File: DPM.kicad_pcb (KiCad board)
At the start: 2 copper layers, 95.9 x 90.2 mm, 19 parts, among them J1 Conn_01x08, U1 74HC590, U2 74HC682, U3 ADG333A, U4 MCP23017_SP, U5 ADG333A

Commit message: + 3 fonctionnalités : PWM, DPM & DDPM + début du routage de la carte
git-svn-id: file:///D%5C00%20-%20Dev%20&%20Calculs%5CRepoTortoiseSVN_PCB%5CD-DPM/trunk@16 f29d8339-a183-0348-962e-9e4594cf8312
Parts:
- removed U1: 74HC590, Package_DIP:DIP-16_W7.62mm_Socket_LongPads
- removed U2: 74HC682, Package_DIP:DIP-20_W7.62mm_Socket_LongPads
- added JP1: Jumper_3_Open, Connector_PinHeader_2.54mm:PinHeader_1x03_P2.54mm_Vertical, F.Cu at (54.6, 85.4)
- added JP2: Jumper_3_Open, Connector_PinHeader_2.54mm:PinHeader_1x03_P2.54mm_Vertical, F.Cu at (54.6, 80.8)
- added JP3: Jumper_3_Open, Connector_PinHeader_2.54mm:PinHeader_1x03_P2.54mm_Vertical, F.Cu at (54.6, 76.2)
- added U25: 74LS85, Package_DIP:DIP-16_W7.62mm_Socket, F.Cu at (121.9, 66.0)
- added U28: 74LS85, Package_DIP:DIP-16_W7.62mm_Socket, F.Cu at (121.9, 88.9)
- added U31: 74LS85, Package_DIP:DIP-16_W7.62mm_Socket, F.Cu at (121.9, 111.8)
- added U6: ADG333A, Package_DIP:DIP-20_W7.62mm_Socket_LongPads, F.Cu at (229.2, 95.9)
- added U8: 4040, Package_DIP:DIP-16_W7.62mm_Socket, F.Cu at (73.7, 71.1)
- J1: value Conn_01x08 -> Conn_02x12_Odd_Even; footprint Connector_PinHeader_2.54mm:PinHeader_1x08_P2.54mm_Vertical -> Connector_PinHeader_2.54mm:PinHeader_2x12_P2.54mm_Vertical
- moved U3 127.8 mm to (229.2, 65.4)
- moved U5 120.8 mm to (229.2, 80.6)
- moved U4 62.7 mm to (73.7, 111.8), turned to 180 degrees
- moved J1 12.7 mm to (86.4, 50.8), turned to 0 degrees
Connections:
- J1 pad 1: DPM -> /Q0
- J1 pad 2: Dyadic DPM -> /CNT_A0
- J1 pad 3: Gray DPM -> /CNT_A11
- J1 pad 4: unconnected-(J1-Pin_4-Pad4) -> /Q11
- J1 pad 5: unconnected-(J1-Pin_5-Pad5) -> /Q1
- J1 pad 6: I2C_A2 -> /CNT_A1
- J1 pad 7: I2C_A1 -> /CNT_A10
- J1 pad 8: I2C_A0 -> /Q10
- PCIe_SPI_1 pad 22: /Connection PCI CAN Express/~{RESET} -> ~{Reset}
- U3 pad 1: /Q6 -> unconnected-(U3-IN1-Pad1)
- U3 pad 10: /Q5 -> unconnected-(U3-IN2-Pad10)
- U3 pad 11: /Q4 -> unconnected-(U3-IN3-Pad11)
- U3 pad 12: /B3 -> /A3
- U3 pad 19: /B0 -> /A0
- U3 pad 2: /B1 -> /A1
- U3 pad 20: /Q7 -> unconnected-(U3-IN4-Pad20)
- U3 pad 9: /B2 -> /A2
- U4 pad 1: /B0 -> /A8
- U4 pad 15: I2C_A0 -> Net-(JP3-C)
- U4 pad 16: I2C_A1 -> Net-(JP2-C)
- U4 pad 17: I2C_A2 -> Net-(JP1-C)
- U4 pad 18: VCC -> ~{Reset}
- U4 pad 2: /B1 -> /A9
- U4 pad 21: Net-(U2-Q0) -> /A0
- U4 pad 22: Net-(U2-Q1) -> /A1
- U4 pad 23: Net-(U2-Q2) -> /A2
- U4 pad 24: Net-(U2-Q3) -> /A3
- U4 pad 25: Net-(U2-Q4) -> /A4
- U4 pad 26: Net-(U2-Q5) -> /A5
- U4 pad 27: Net-(U2-Q6) -> /A6
- U4 pad 28: Net-(U2-Q7) -> /A7
- U4 pad 3: /B2 -> /A10
- U4 pad 4: /B3 -> /A11
- U4 pad 5: /B4 -> PreScaler0
- U4 pad 6: /B5 -> PreScaler1
- U4 pad 7: /B6 -> PreScaler2
- U4 pad 8: /B7 -> ~{CntEN}
- U5 pad 1: /Q0 -> unconnected-(U5-IN1-Pad1)
- U5 pad 10: /Q3 -> unconnected-(U5-IN2-Pad10)
- U5 pad 11: /Q2 -> unconnected-(U5-IN3-Pad11)
- U5 pad 12: /B5 -> /A7
- U5 pad 17: Net-(U5-D3) -> Net-(U3-D3)
- U5 pad 19: /B6 -> /A4
- U5 pad 2: /B7 -> /A5
- U5 pad 20: /Q1 -> unconnected-(U5-IN4-Pad20)
- U5 pad 3: Dyadic DPM -> Net-(U5-D1)
- U5 pad 7: Net-(U3-D3) -> Net-(U5-D1)
- U5 pad 9: /B4 -> /A6
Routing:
- net Ground: track 421.7 -> 211.3 mm
- net VCC: track 326.1 -> 161.0 mm
- net /A11: track 0.00 -> 110.9 mm
- net /A0: track 0.00 -> 92.1 mm
- net /CNT_A11: track 0.00 -> 91.2 mm
- net /B5: track 90.9 -> 0.00 mm
- net /A1: track 0.00 -> 89.2 mm
- net /A3: track 0.00 -> 87.3 mm
- net /B3: track 85.5 -> 0.00 mm
- net /A2: track 0.00 -> 84.1 mm
- net /A9: track 0.00 -> 82.9 mm
- net /B1: track 82.1 -> 0.00 mm
- net /B0: track 80.8 -> 0.00 mm
- net /CNT_A10: track 0.00 -> 79.4 mm
- net Dyadic DPM: track 79.4 -> 0.00 mm
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- added copper zone on F.Cu, net Ground
- removed copper zone on F.Cu, net VCC
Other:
- board text removed: "COPI"

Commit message: POPOPO !!!!! 1ere version du routage de la carte
git-svn-id: file:///D%5C00%20-%20Dev%20&%20Calculs%5CRepoTortoiseSVN_PCB%5CD-DPM/trunk@17 f29d8339-a183-0348-962e-9e4594cf8312
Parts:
- removed PCIe_CAN_1: Conn_02x07_Odd_Even, Connector_PinHeader_2.54mm:PinHeader_2x07_P2.54mm_Vertical
- removed PCIe_SPI_1: Conn_02x11_Odd_Even, Connector_PinHeader_2.54mm:PinHeader_2x11_P2.54mm_Vertical
- added JP4: IDC-14, Connector_IDC:IDC-Header_2x07_P2.54mm_Horizontal, F.Cu at (58.4, 114.3)
- moved U3 113.7 mm to (116.8, 48.3), turned to 0 degrees
- moved U6 112.7 mm to (116.8, 104.1), turned to 0 degrees
- moved U5 112.5 mm to (116.8, 76.2), turned to 0 degrees
- moved U25 13.0 mm to (109.2, 68.6)
- moved U28 13.0 mm to (109.2, 91.4)
- moved U31 13.0 mm to (109.2, 114.3)
- moved R5 7.57 mm to (72.7, 118.1)
- moved LED1 6.67 mm to (66.0, 118.1)
- moved JP1 6.43 mm to (48.3, 86.4)
- moved JP2 6.37 mm to (48.3, 81.3)
- moved JP3 6.35 mm to (48.3, 76.2)
- moved U4 5.08 mm to (78.7, 111.8)
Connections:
- net VCC renamed +5V
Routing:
- net Ground: track 211.3 -> 541.8 mm
- net +5V: track 161.0 -> 399.4 mm
- net DPM: track 0.00 -> 51.0 mm
- net /A9: track 82.9 -> 43.7 mm
- net /A11: track 110.9 -> 75.0 mm
- net Clock: track 37.9 -> 65.1 mm
- net /A8: track 57.7 -> 80.8 mm
- net ~{Reset}: track 20.7 -> 40.7 mm
- net /A5: track 77.3 -> 60.9 mm
- net unconnected-(U3-IN4-Pad20): track 16.3 -> 0.00 mm
- net unconnected-(U6-IN3-Pad11): track 16.3 -> 0.00 mm
- net /CNT_A3: track 26.5 -> 12.7 mm
- net /CNT_A2: track 26.5 -> 12.7 mm
- net Net-(JP2-C): track 10.1 -> 23.5 mm
- net /CNT_A11: track 91.2 -> 78.1 mm
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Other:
- board text removed: "+3.3V"
- board text removed: "CAN0 H"
- board text removed: "CAN0 L"
- board text removed: "CAN1 H"
- board text removed: "CAN1 L"
- board text removed: "CIPO"
- board text removed: "OSC1"
- board text removed: "OSC2"
- board text removed: "SCLK"
- board text removed: "~{CS1}"
- board text removed: "~{CS2}"
- board text removed: "~{CS3}"

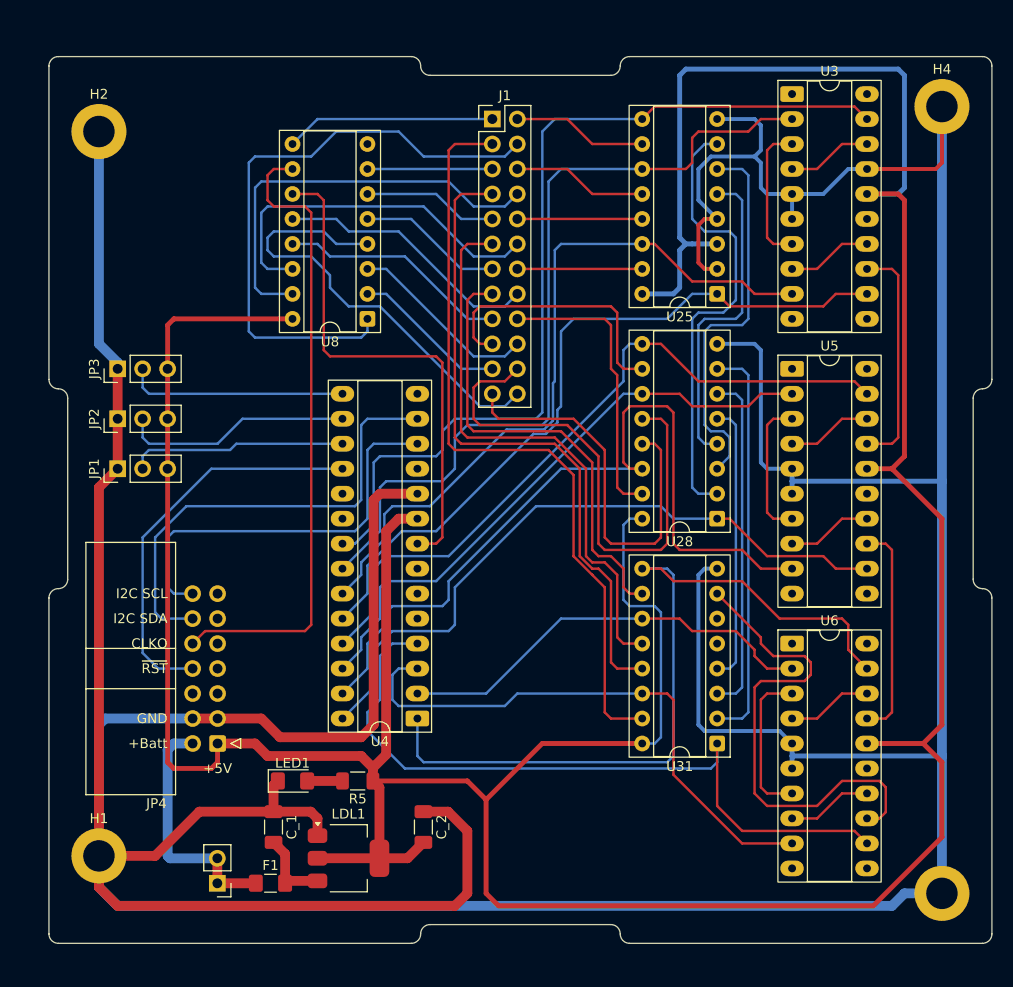
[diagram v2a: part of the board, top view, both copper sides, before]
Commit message: Ajout du prescaler TODO : - condensateurs de découplage - bouchon I2C
git-svn-id: file:///D%5C00%20-%20Dev%20&%20Calculs%5CRepoTortoiseSVN_PCB%5CD-DPM/trunk@18 f29d8339-a183-0348-962e-9e4594cf8312
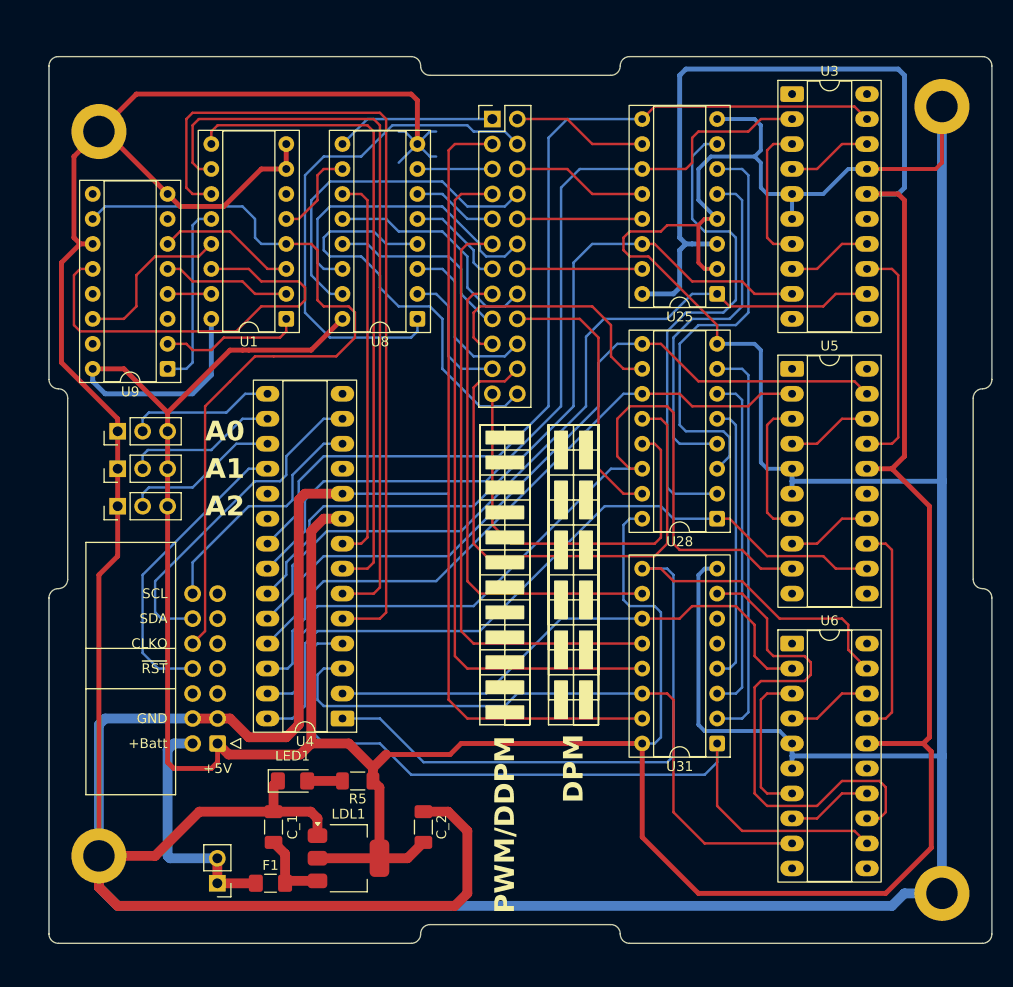
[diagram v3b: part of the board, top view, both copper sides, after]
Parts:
- added U1: 74LS251, Package_DIP:DIP-16_W7.62mm_Socket, F.Cu at (65.4, 71.1)
- added U9: 4040, Package_DIP:DIP-16_W7.62mm_Socket, F.Cu at (53.3, 76.2)
- moved U4 7.62 mm to (71.1, 111.8)
- moved JP3 6.35 mm to (48.3, 82.5)
- moved JP2 5.08 mm to (48.3, 86.4)
- moved U8 5.08 mm to (78.7, 71.1)
- moved JP1 3.81 mm to (48.3, 90.2)
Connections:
- U8 pad 10: Clock -> Net-(U1-Y)
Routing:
- net Ground: track 541.8 -> 650.9 mm
- net PreScaler0: track 0.00 -> 85.5 mm
- net PreScaler1: track 0.00 -> 76.6 mm
- net PreScaler2: track 0.00 -> 65.6 mm
- net /Div_512: track 0.00 -> 43.9 mm
- net /Div_4096: track 0.00 -> 18.9 mm
- net /Div_1024: track 0.00 -> 17.1 mm
- net SCL: track 41.3 -> 24.9 mm
- net Clock: track 65.1 -> 81.1 mm
- net /Div_64: track 0.00 -> 14.4 mm
- net /Div_8: track 0.00 -> 14.2 mm
- net SDA: track 47.8 -> 34.3 mm
- net /Div_16: track 0.00 -> 13.1 mm
- net ~{CntEN}: track 51.9 -> 39.9 mm
- net /A9: track 43.7 -> 53.9 mm
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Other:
- board text added: "A0"
- board text added: "A1"
- board text added: "A2"
- board text added: "DPM"
- board text added: "PWM/DDPM"
- board text added: "SCL"
- board text added: "SDA"
- board text removed: "I2C SCL"
- board text removed: "I2C SDA"

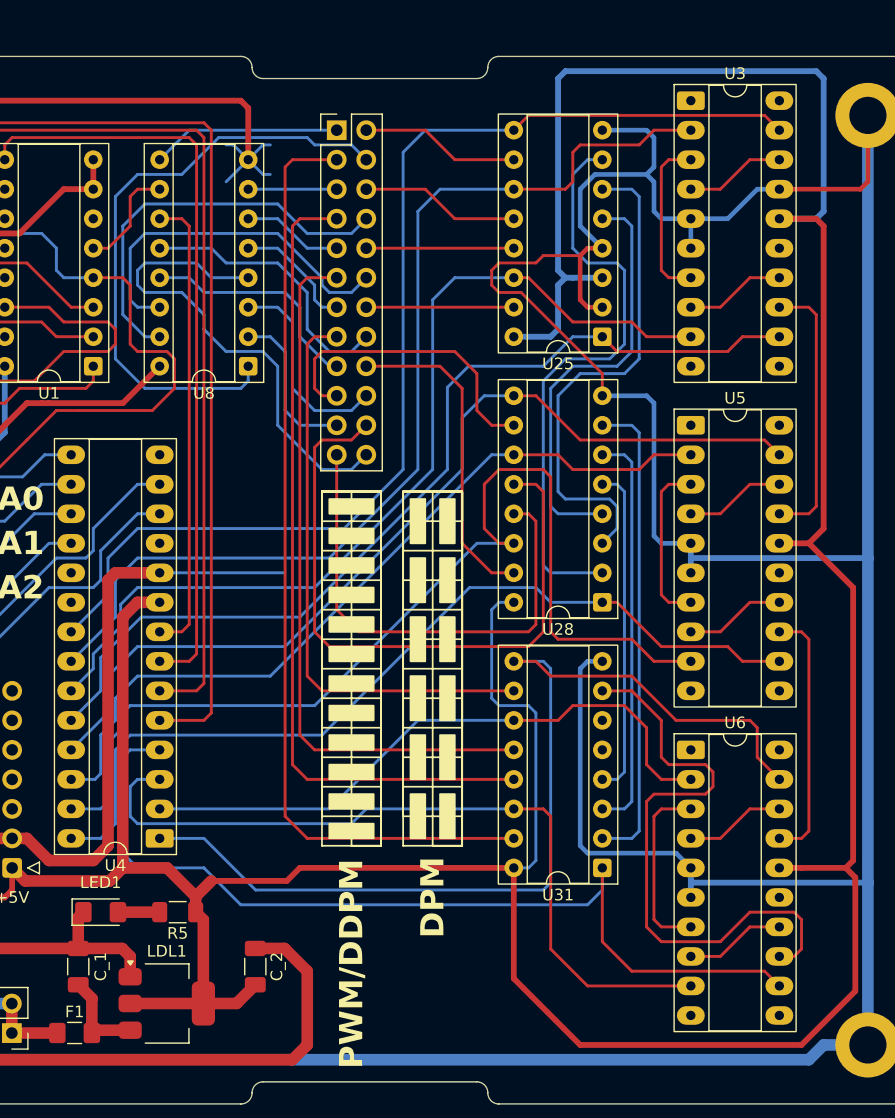
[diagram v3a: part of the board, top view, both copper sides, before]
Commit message: Début de ré&vision pour ajouter des câblages
git-svn-id: file:///D%5C00%20-%20Dev%20&%20Calculs%5CRepoTortoiseSVN_PCB%5CD-DPM/trunk@19 f29d8339-a183-0348-962e-9e4594cf8312
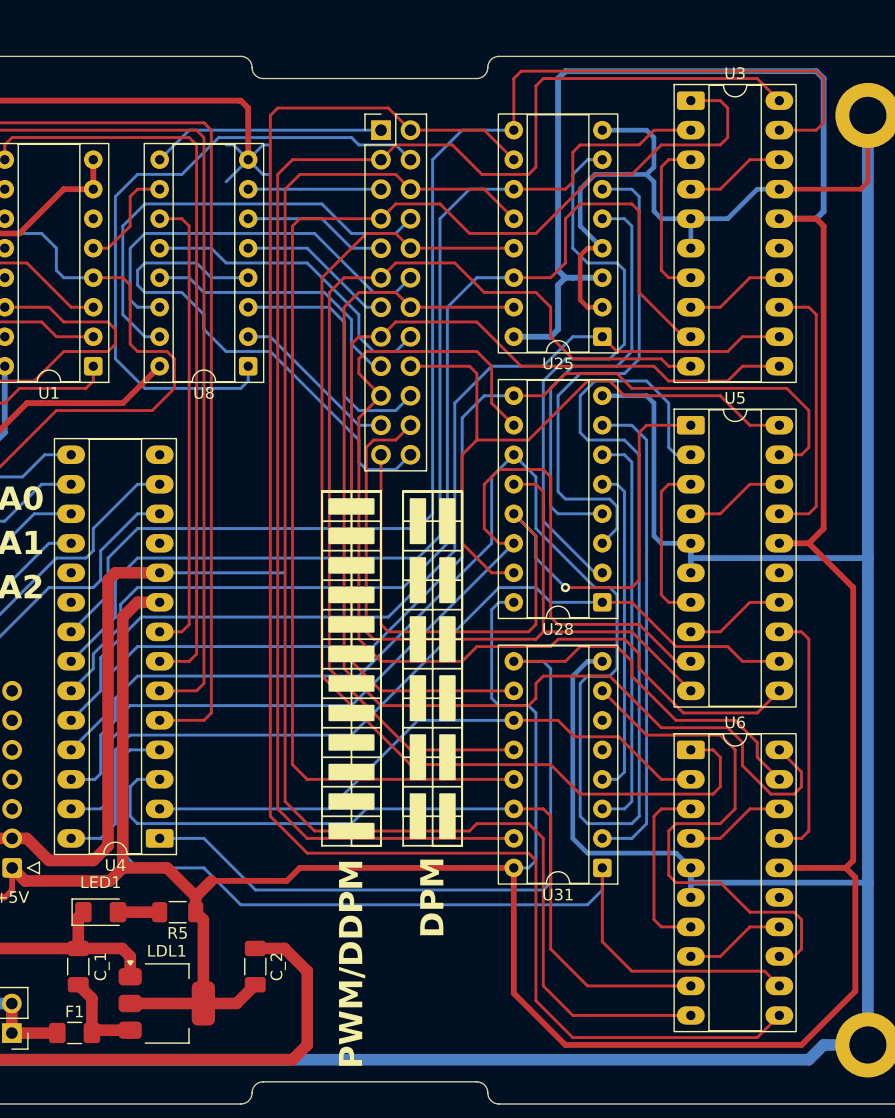
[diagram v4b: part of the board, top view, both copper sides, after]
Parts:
- moved J1 3.81 mm to (90.2, 50.8)
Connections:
- U3 pad 1: unconnected-(U3-IN1-Pad1) -> /CNT_A10
- U3 pad 10: unconnected-(U3-IN2-Pad10) -> /CNT_A9
- U3 pad 11: unconnected-(U3-IN3-Pad11) -> /CNT_A8
- U3 pad 20: unconnected-(U3-IN4-Pad20) -> /CNT_A11
- U5 pad 1: unconnected-(U5-IN1-Pad1) -> /CNT_A6
- U5 pad 10: unconnected-(U5-IN2-Pad10) -> /CNT_A5
- U5 pad 11: unconnected-(U5-IN3-Pad11) -> /CNT_A4
- U5 pad 20: unconnected-(U5-IN4-Pad20) -> /CNT_A7
- U6 pad 1: unconnected-(U6-IN1-Pad1) -> /CNT_A2
- U6 pad 10: unconnected-(U6-IN2-Pad10) -> /CNT_A1
- U6 pad 11: unconnected-(U6-IN3-Pad11) -> /CNT_A0
- U6 pad 20: unconnected-(U6-IN4-Pad20) -> /CNT_A3
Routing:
- net /CNT_A0: track 13.8 -> 142.9 mm
- net /CNT_A1: track 13.8 -> 125.0 mm
- net /CNT_A3: track 12.7 -> 98.9 mm
- net /A5: track 69.0 -> 154.7 mm
- net /CNT_A2: track 12.7 -> 97.0 mm
- net /CNT_A4: track 26.6 -> 85.7 mm
- net /CNT_A11: track 81.1 -> 130.2 mm
- net /CNT_A10: track 70.0 -> 114.6 mm
- net /CNT_A8: track 49.7 -> 82.6 mm
- net /CNT_A7: track 27.9 -> 56.3 mm
- net /CNT_A6: track 42.6 -> 71.0 mm, vias 0 -> 1
- net /CNT_A9: track 61.1 -> 88.5 mm
- net Ground: track 650.9 -> 627.4 mm
- net /A0: track 97.8 -> 115.2 mm
- net /A2: track 80.6 -> 95.5 mm
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
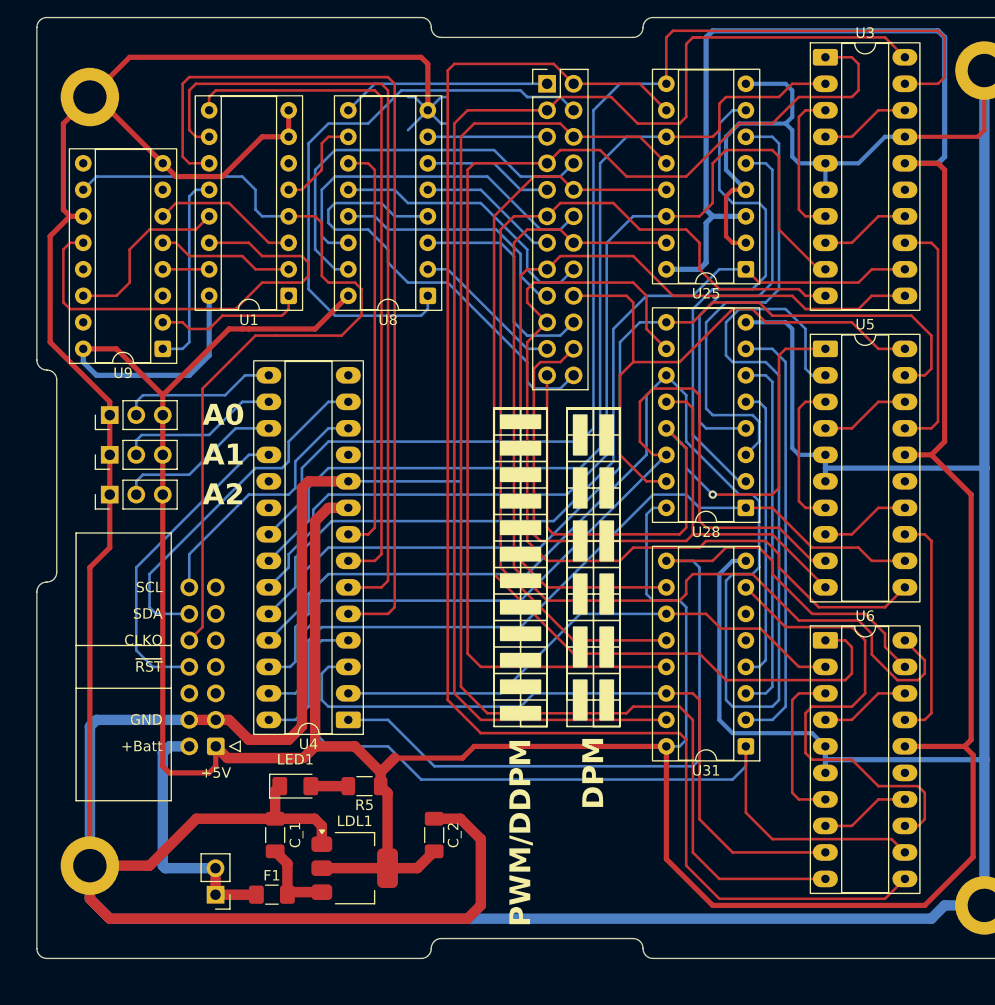
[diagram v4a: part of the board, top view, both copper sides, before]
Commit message: Ajout pistes An sur DDPM Suppression du via des enfers Ajout jumpers pour DPM sur connecteur IDC-14 Début du silksreen
TODO : 
- condensateurs de découplage
- bouchon I2C

git-svn-id: file:///D%5C00%20-%20Dev%20&%20Calculs%5CRepoTortoiseSVN_PCB%5CD-DPM/trunk@20 f29d8339-a183-0348-962e-9e4594cf8312
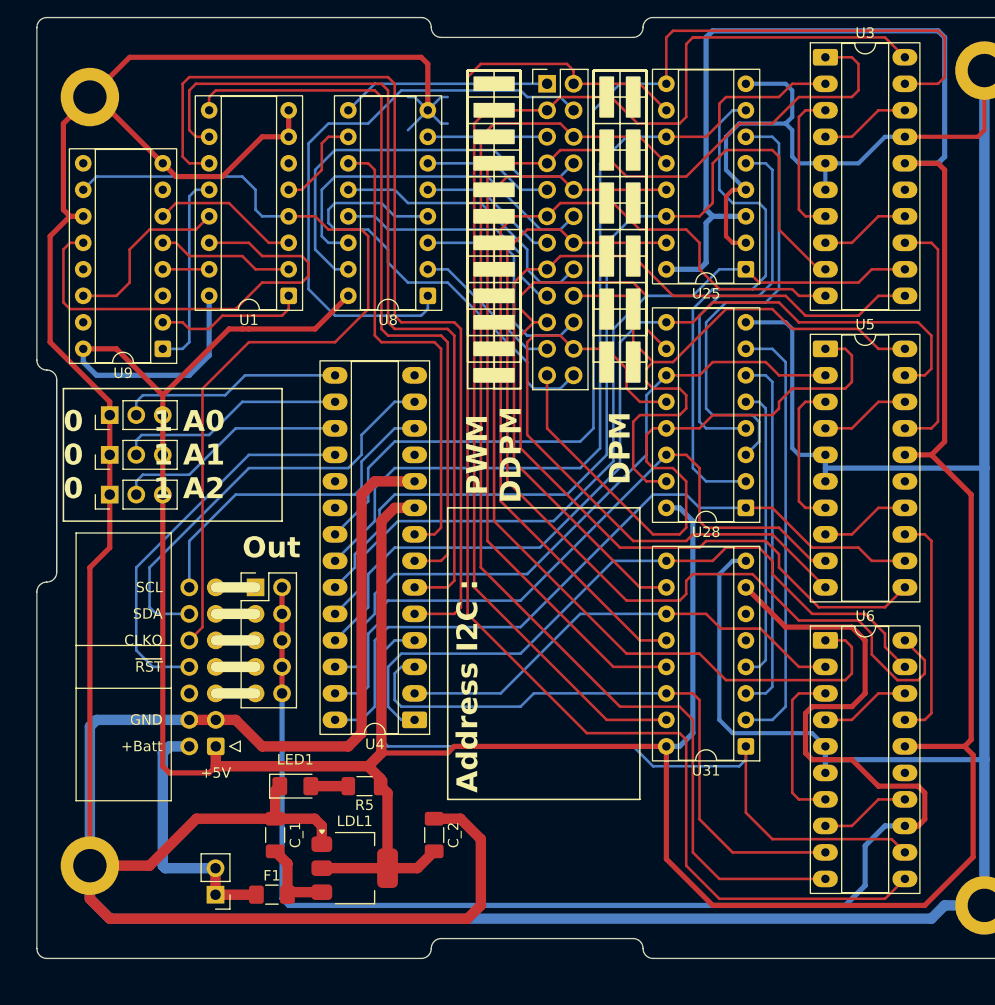
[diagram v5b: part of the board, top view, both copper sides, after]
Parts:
- added J2: Conn_02x05_Odd_Even, Connector_PinHeader_2.54mm:PinHeader_2x05_P2.54mm_Vertical, F.Cu at (62.2, 99.1)
- moved U4 6.35 mm to (77.5, 111.8)
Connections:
- JP4 pad 11: unconnected-(JP4-Pin_11-Pad11) -> Net-(J2-Pin_3)
- JP4 pad 13: unconnected-(JP4-Pin_13-Pad13) -> Net-(J2-Pin_1)
- JP4 pad 5: unconnected-(JP4-Pin_5-Pad5) -> Net-(J2-Pin_9)
- JP4 pad 7: unconnected-(JP4-Pin_7-Pad7) -> Net-(J2-Pin_7)
- JP4 pad 9: unconnected-(JP4-Pin_9-Pad9) -> Net-(J2-Pin_5)
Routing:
- net DPM: track 46.6 -> 141.8 mm
- net /A5: track 154.7 -> 66.0 mm
- net /A6: track 90.4 -> 67.4 mm
- net /A8: track 87.2 -> 67.4 mm
- net /CNT_A1: track 125.0 -> 114.0 mm
- net /CNT_A10: track 114.6 -> 104.5 mm
- net /CNT_A11: track 130.2 -> 120.4 mm
- net /CNT_A6: track 71.0 -> 62.0 mm, vias 1 -> 0
- net /CNT_A0: track 142.9 -> 134.7 mm
- net /A11: track 80.4 -> 72.6 mm
- net /A10: track 67.4 -> 59.8 mm
- net SCL: track 24.9 -> 32.0 mm
- net /A1: track 91.6 -> 84.9 mm
- net SDA: track 34.3 -> 41.0 mm
- net /A7: track 76.3 -> 69.9 mm
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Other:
- board text added: "0 1 A0 0 1 A1 0 1 A2"
- board text added: "Address I2C :"
- board text added: "Out"
- board text added: "PWM DDPM"
- board text removed: "A0"
- board text removed: "A1"
- board text removed: "A2"
- board text removed: "PWM/DDPM"
